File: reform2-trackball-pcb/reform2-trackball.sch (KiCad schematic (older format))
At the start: 42 parts, among them J1 Conn_USB, J2 Conn_01x06_Female, SW1 Choc, SW2 Choc, SW3 Choc, SW4 Choc, SW5 Choc, SW6 SW_RST, SW7 SW_HWB, U1 ATmega32U2-AU, U2 TLV75533PDBV, Y1 Crystal_GND24

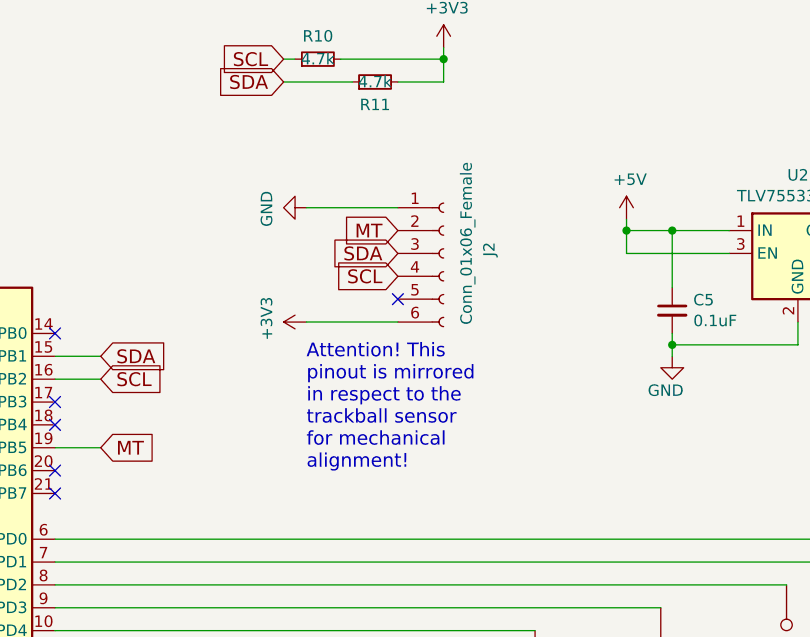
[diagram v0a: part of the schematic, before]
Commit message: Hardware changes for the mouse-trak
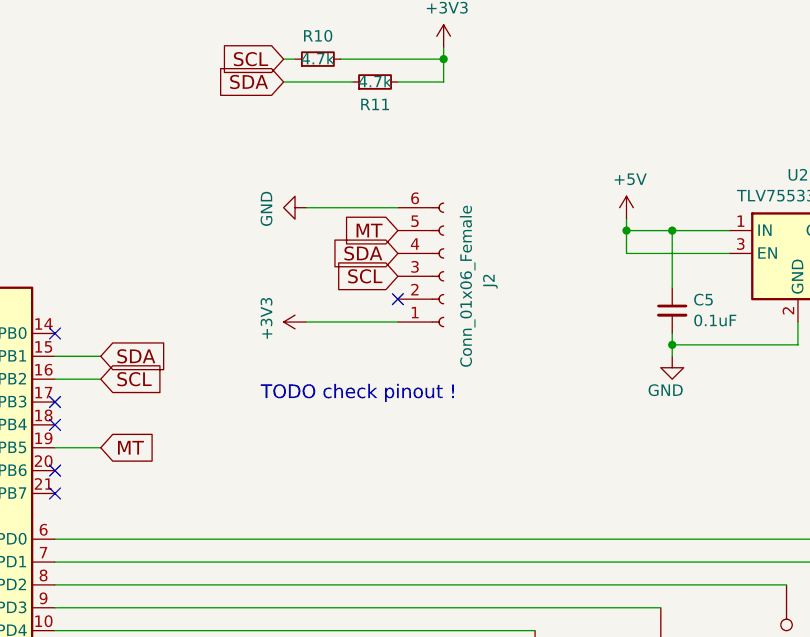
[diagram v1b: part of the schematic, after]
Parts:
- J2: footprint Connector_FFC-FPC:Hirose_FH12-6S-0.5SH_1x06-1MP_P0.50mm_Horizontal -> Connector_PinSocket_2.54mm:PinSocket_1x06_P2.54mm_Vertical
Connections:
- net +3V3: now also J2.1 (Pin_1); no longer J2.6 (Pin_6)
- net GND: now also J2.6 (Pin_6); no longer J2.1 (Pin_1)
- net MT: now also J2.5 (Pin_5); no longer J2.2 (Pin_2)
- net SCL: now also J2.3 (Pin_3); no longer J2.4 (Pin_4)
- net SDA: now also J2.4 (Pin_4); no longer J2.3 (Pin_3)
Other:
- note added: "TODO check pinout !"
- note removed: "Attention! This\npinout is mirrored\nin respect to the \ntrackball sensor\nfor mechanical\nalignment!"
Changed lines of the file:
@@
 L Connector:Conn_01x06_Female J2
 U 1 1 5D3375CD
-P 7000 2000
-F 0 "J2" V 7200 2050 50  0000 R CNN
-F 1 "Conn_01x06_Female" V 7100 2400 50  0000 R CNN
-F 2 "Connector_FFC-FPC:Hirose_FH12-6S-0.5SH_1x06-1MP_P0.50mm_Horizontal" H 7000 2000 50  0001 C CNN
-F 3 "~" H 7000 2000 50  0001 C CNN
-F 4 "Hirose" H 7000 2000 50  0001 C CNN "Manufacturer"
-F 5 "FH12-6S-0.5SH(55)" H 7000 2000 50  0001 C CNN "Manufacturer_No"
-	1    7000 2000
-	1    0    0    -1
+P 7000 2100
+F 0 "J2" V 7200 2150 50  0000 R CNN
+F 1 "Conn_01x06_Female" V 7100 2500 50  0000 R CNN
+F 2 "Connector_PinSocket_2.54mm:PinSocket_1x06_P2.54mm_Vertical" H 7000 2100 50  0001 C CNN
+F 3 "~" H 7000 2100 50  0001 C CNN
+F 4 "Hirose" H 7000 2100 50  0001 C CNN "Manufacturer"
+F 5 "FH12-6S-0.5SH(55)" H 7000 2100 50  0001 C CNN "Manufacturer_No"
+	1    7000 2100
+	1    0    0    1
 $EndComp
 Text GLabel 6800 2000 0    60   Input ~ 0
@@
 F 5 "CPG135001D02" H 7950 3900 50  0001 C CNN "Manufacturer_No"
 	1    7950 3900
-	1    0    0    -1
-$EndComp
-$Comp
-L reform-trackball:Choc SW1
-U 1 1 5D501AF4
-P 7400 4000
-F 0 "SW1" H 7598 4121 50  0000 L CNN
-F 1 "Choc" H 7598 4030 50  0000 L CNN
-F 2 "keyswitches:PG1350" H 7400 4000 50  0001 C CNN
-F 3 "" H 7400 4000 50  0000 C CNN
-F 4 "Kailh" H 7400 4000 50  0001 C CNN "Manufacturer"
-F 5 "CPG135001D02" H 7400 4000 50  0001 C CNN "Manufacturer_No"
-	1    7400 4000
 	1    0    0    -1
 $EndComp
@@
 	0    1    1    0
 $EndComp
-Text Notes 6400 2950 0    60   ~ 0
-Attention! This\npinout is mirrored\nin respect to the \ntrackball sensor\nfor mechanical\nalignment!
+Text Notes 6200 2650 0    60   ~ 0
+TODO check pinout !
+$Comp
+L reform-trackball:Choc SW1
+U 1 1 5D501AF4
+P 7400 4000
+F 0 "SW1" H 7598 4121 50  0000 L CNN
+F 1 "Choc" H 7598 4030 50  0000 L CNN
+F 2 "keyswitches:PG1350" H 7400 4000 50  0001 C CNN
+F 3 "" H 7400 4000 50  0000 C CNN
+F 4 "Kailh" H 7400 4000 50  0001 C CNN "Manufacturer"
+F 5 "CPG135001D02" H 7400 4000 50  0001 C CNN "Manufacturer_No"
+	1    7400 4000
+	1    0    0    -1
+$EndComp
 $EndSCHEMATC
